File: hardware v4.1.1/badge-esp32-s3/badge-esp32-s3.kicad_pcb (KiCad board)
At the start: 2 copper layers, 131.5 x 83.5 mm, 218 parts, among them CN1 B4B-PH-SM4-TB (LF)(SN), J1 Connector, USB-TYPE-C-16P, J11 Conn_02x03_Odd_Even, J12 Conn_01x02_Socket, J13 Conn_01x04_Socket, J14 Conn_01x02_Socket, J15 Conn_01x02_Socket, J2 Connector, USB-TYPE-C-16P, J3 Conn_02x06_Odd_Even, J4 Conn_02x15_Odd_Even, J5 Conn_01x02_Socket, J6 Conn_01x04_Socket, J7 Conn_01x08_Socket, J8 Conn_01x08_Socket, J9 Conn_02x06_Odd_Even, P1 PH-2A_C2319, P2 FPC 0.5MM 12P Pull type H2.0m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, P3 WJ124-3.81-2P, Q1 SS8050 200-350, Q10 DMN3150L-7, Q2 SS8050 200-350, Q3 AP1606, Q5 DTC114E, Q7 AO3415_C54938718, Q8 AO3415_C54938718, Q9 AO3415_C54938718, SW1 TS-1088-AR02016, SW10 SK22D02G5, SW2 TS-1088-AR02016, SW4 TS665CJ, SW5 TS665CJ, SW6 TS665CJ, SW7 TS665CJ, SW8 TS665CJ, SW9 TS665CJ, U1 ESP32-S3-MINI-1-N4R2, U11 SY6288F1ABC, U12 SY6288F1ABC, U18 MMA8452QR1_C11360, U2 TPS630701RNMR, U3 CP2102N-A02-GQFN28R, U4 TP4056, U5 TPS2121RUXR, U6 ZX-SH1.0-4PWT, U7 HS20HS072RX-fpc, U8 TUSB321AIRWBR, U9 AP63201WU-7

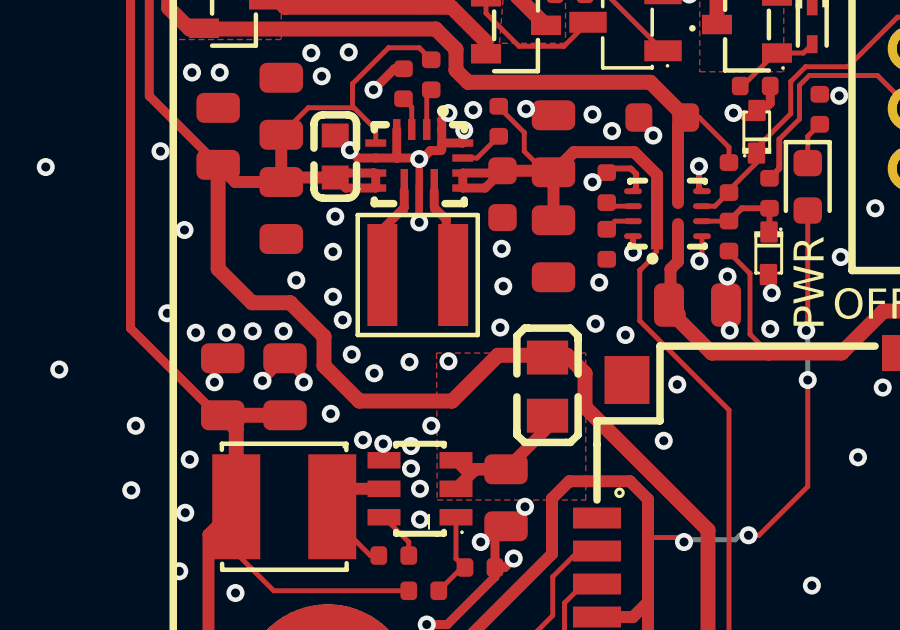
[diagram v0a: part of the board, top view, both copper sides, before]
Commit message: fixed out of stock components
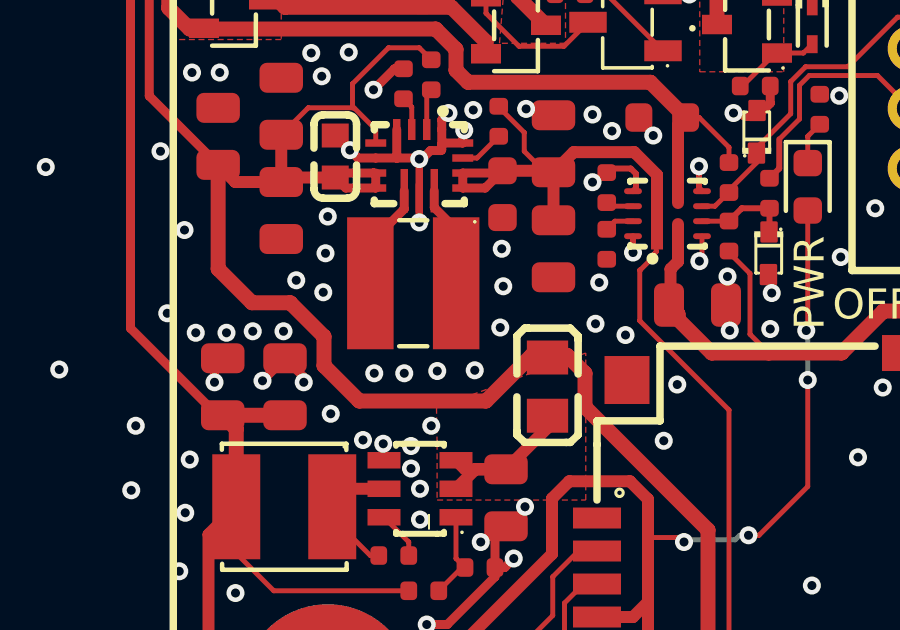
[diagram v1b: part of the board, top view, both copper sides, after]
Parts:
- removed L3: XGL4020-152MEC, lcsc-lib:IND-SMD_L4.0-W4.0_XEL4020
- added L4: FTC404020S1R5MGCA, lcsc-lib:IND-SMD_L4.1-W4.1_SPM40XX, F.Cu at (190.3, 108.0)
- R64: value 75kΩ -> 0Ω
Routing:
- net GND: vias 392 -> 391

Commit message: changed 3.3V reg from adj to fixed
changed 3.3V reg from adj to fixed and reflexed that in the bom
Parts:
- U9: value AP63201WU-7 -> AP63203WU-7
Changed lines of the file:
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@@
 			)
 		)
-		(property "Value" "AP63201WU-7"
+		(property "Value" "AP63203WU-7"
 			(at 0 5.2 90)
 			(layer "F.Fab")
@@
 			)
 		)
-		(property "LCSC Part" "C2071044"
+		(property "LCSC Part" "C780769"
 			(at 0 0 90)
 			(layer "F.Fab")
@@
 			)
 		)
-		(property "MPN" "AP63201WU-7"
+		(property "MPN" "AP63203WU-7"
 			(at 0 0 90)
 			(unlocked yes)

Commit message: changed silkscreen for LED references
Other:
- board text added: "RGB LED"
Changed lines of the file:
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@@
 			(at 0 -1.43 90)
 			(layer "F.SilkS")
+			(hide yes)
 			(effects
 				(font
@@
 			(at 0 1.43 90)
 			(layer "F.Fab")
+			(hide yes)
 			(effects
 				(font
@@
 			(at 0.124 2.518 90)
 			(layer "F.SilkS")
+			(hide yes)
 			(effects
 				(font
@@
 		)
 	)
+	(gr_text "LED"
+		(at 117.344341 119.469919 90)
+		(layer "F.Fab")
+		(effects
+			(font
+				(size 1 1)
+				(thickness 0.15)
+			)
+		)
+	)
+	(gr_text "RGB LED"
+		(at 110.813489 119.767087 90)
+		(layer "F.Fab")
+		(effects
+			(font
+				(size 1 1)
+				(thickness 0.15)
+			)
+		)
+	)
